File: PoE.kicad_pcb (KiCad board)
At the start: 4 copper layers, 102.5 x 35 mm, 106 parts, among them J1 Conn_01x03, J1001 8P8C_LED_Shielded_x2, J1002 8P8C_LED_Shielded_x2, J3001 Conn_01x03, Q2 MMBT3906, Q2001 SI7898DP-T1-E3, U1 TPS563203, U1001 7490220122, U1002 TCMT1107, U2001 TPS23751PWP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

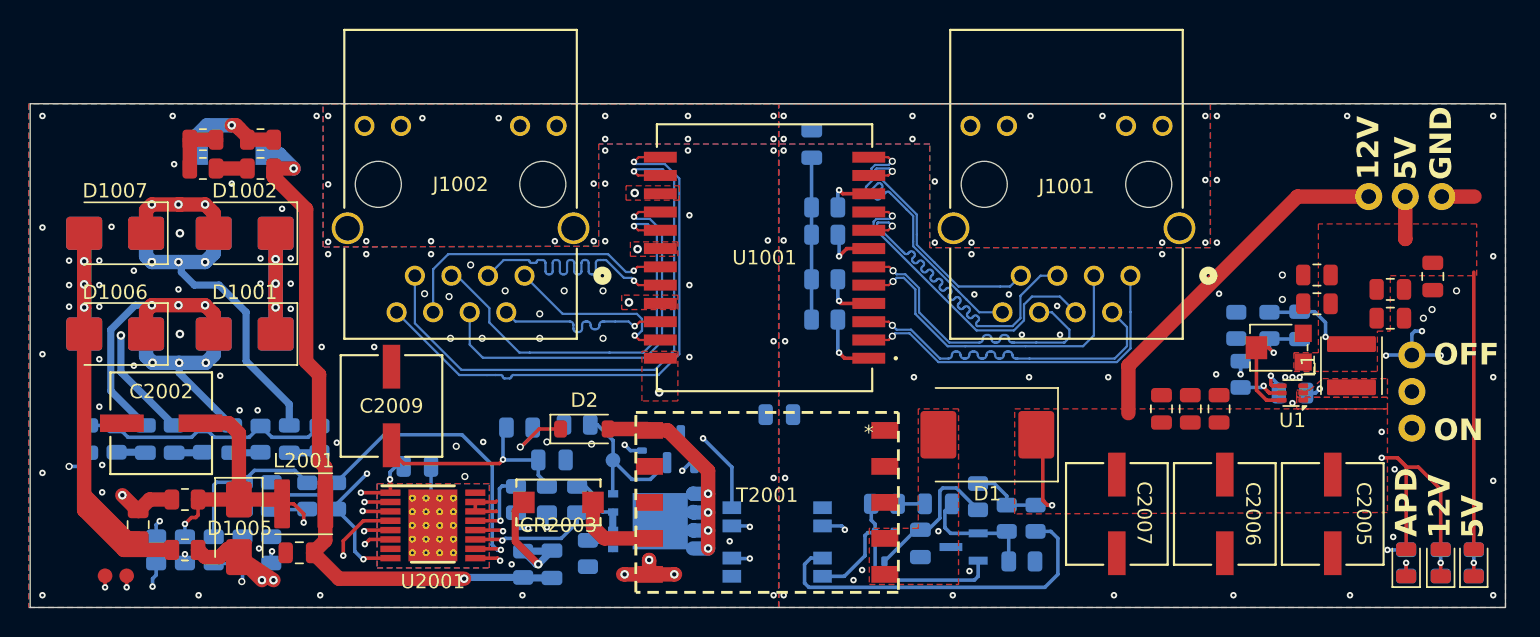
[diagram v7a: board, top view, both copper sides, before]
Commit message: Added BOM, fixed routing mistakes
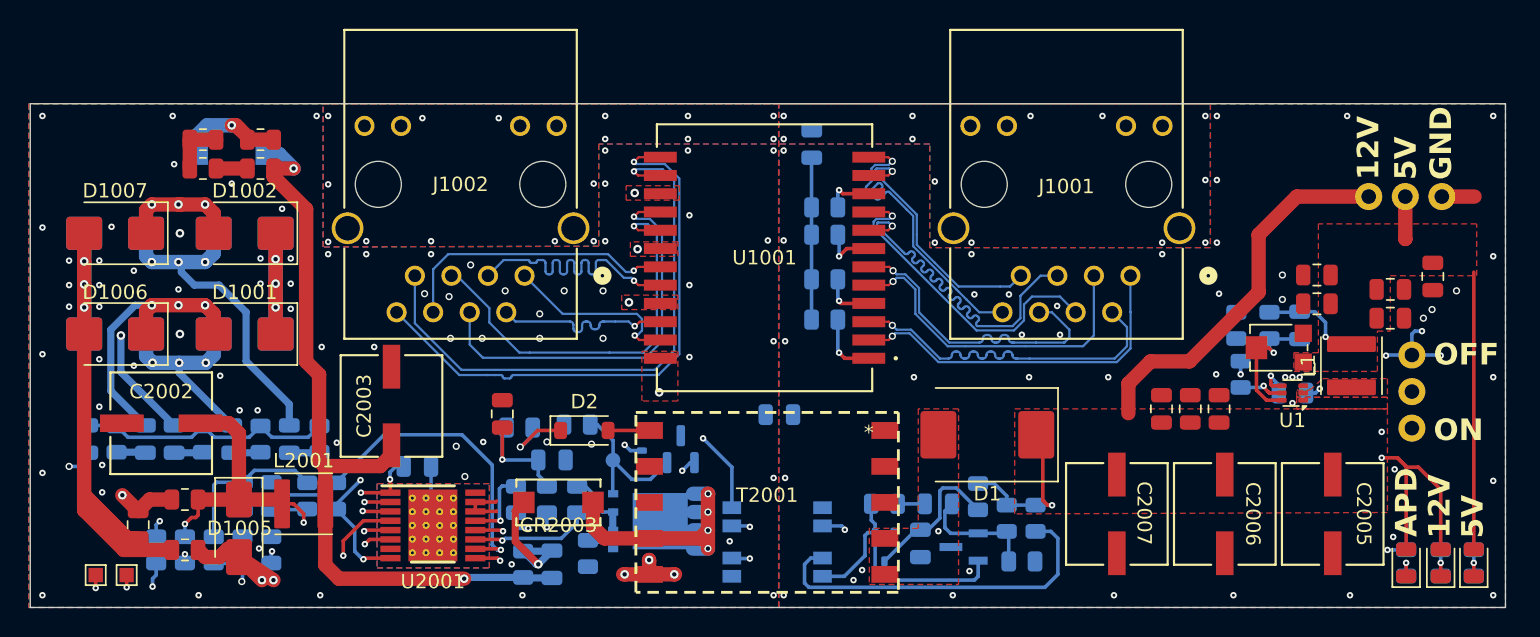
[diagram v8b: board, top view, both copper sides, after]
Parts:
- C2003: footprint Capacitor_SMD:C_0805_2012Metric -> footprints:CAP_WCAP-ASLI_06p3X05p5_WRE
- C2009: footprint footprints:CAP_WCAP-ASLI_06p3X05p5_WRE -> Capacitor_SMD:C_0805_2012Metric
- TP1001, TP1006: footprint SparkFun-Connector:TestPoint-1.0mm -> TestPoint:TestPoint_Pad_1.0x1.0mm
- moved C2003 12.0 mm to (67.6, 44.0), turned to 90 degrees
- moved C2009 7.72 mm to (75.3, 44.5)
- moved TP1001 0.65 mm to (47.0, 55.8)
- moved D2 0.10 mm to (81.0, 45.7)
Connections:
- Q2001 pad D: Net-(D2-A) -> Net-(CR2003-Pad2)
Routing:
- net Net-(D2-A): track 17.5 -> 2.91 mm, vias 4 -> 0
- net Net-(CR2003-Pad2): track 5.93 -> 18.2 mm, vias 0 -> 4
- net VC: track 23.0 -> 16.6 mm
- net /Flyback/T_PRI: track 73.3 -> 78.3 mm
- net +12V: track 57.5 -> 59.1 mm
- net VDD: track 37.2 -> 37.9 mm
- net Net-(U2001-CTL): track 75.0 -> 75.6 mm
